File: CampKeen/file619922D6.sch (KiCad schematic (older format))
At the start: 50 parts, among them Q20 2N7000, Q21 2N7000, Q22 2N7000, Q23 2N7000, Q24 2N7000, Q25 2N7000, Q26 2N7000, Q27 2N7000, Q28 2N7000, Q29 2N7000

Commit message: schematic done for Input isolation updates.
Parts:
- removed D10, D11, D12, D13, D3, D6, D7, D8, D9: 1N4004, Diode_THT:D_DO-41_SOD81_P10.16mm_Horizontal, symbol Diode:1N4004
- removed R70, R71, R72, R76, R77, R78: 1M, Resistor_THT:R_Axial_DIN0207_L6.3mm_D2.5mm_P2.54mm_Vertical, symbol Device:R
- added D? (x9): 1N4007, Diode_THT:D_DO-41_SOD81_P10.16mm_Horizontal, symbol Diode:1N4007
- added IC? (x2): LTV-814, DIP762W60P254L460H450Q4N, symbol SamacSys_Parts:LTV-814
- added Q? (x2): LTV-847, DIP762W60P254L1984H450Q16N, symbol SamacSys_Parts:LTV-847
- added R? (x10): 22k, Resistor_THT:R_Axial_DIN0207_L6.3mm_D2.5mm_P2.54mm_Vertical, symbol Device:R
- added R? (x5): 330, Resistor_THT:R_Axial_DIN0207_L6.3mm_D2.5mm_P2.54mm_Vertical, symbol Device:R
- added R?: 300, Resistor_THT:R_Axial_DIN0207_L6.3mm_D2.5mm_P2.54mm_Vertical, symbol Device:R
- D5: value 1N4004 -> 1N4007; symbol Diode:1N4004 -> Diode:1N4007
- R63, R64, R66: value 1M -> 330
- R65: value 1M -> 300
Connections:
- net labels added: +5V
- wire segments 129 -> 207
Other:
- moved on the sheet: C28, C29, C30, C31, C32, C33, C34, C35, C36, C37, D5, Q20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

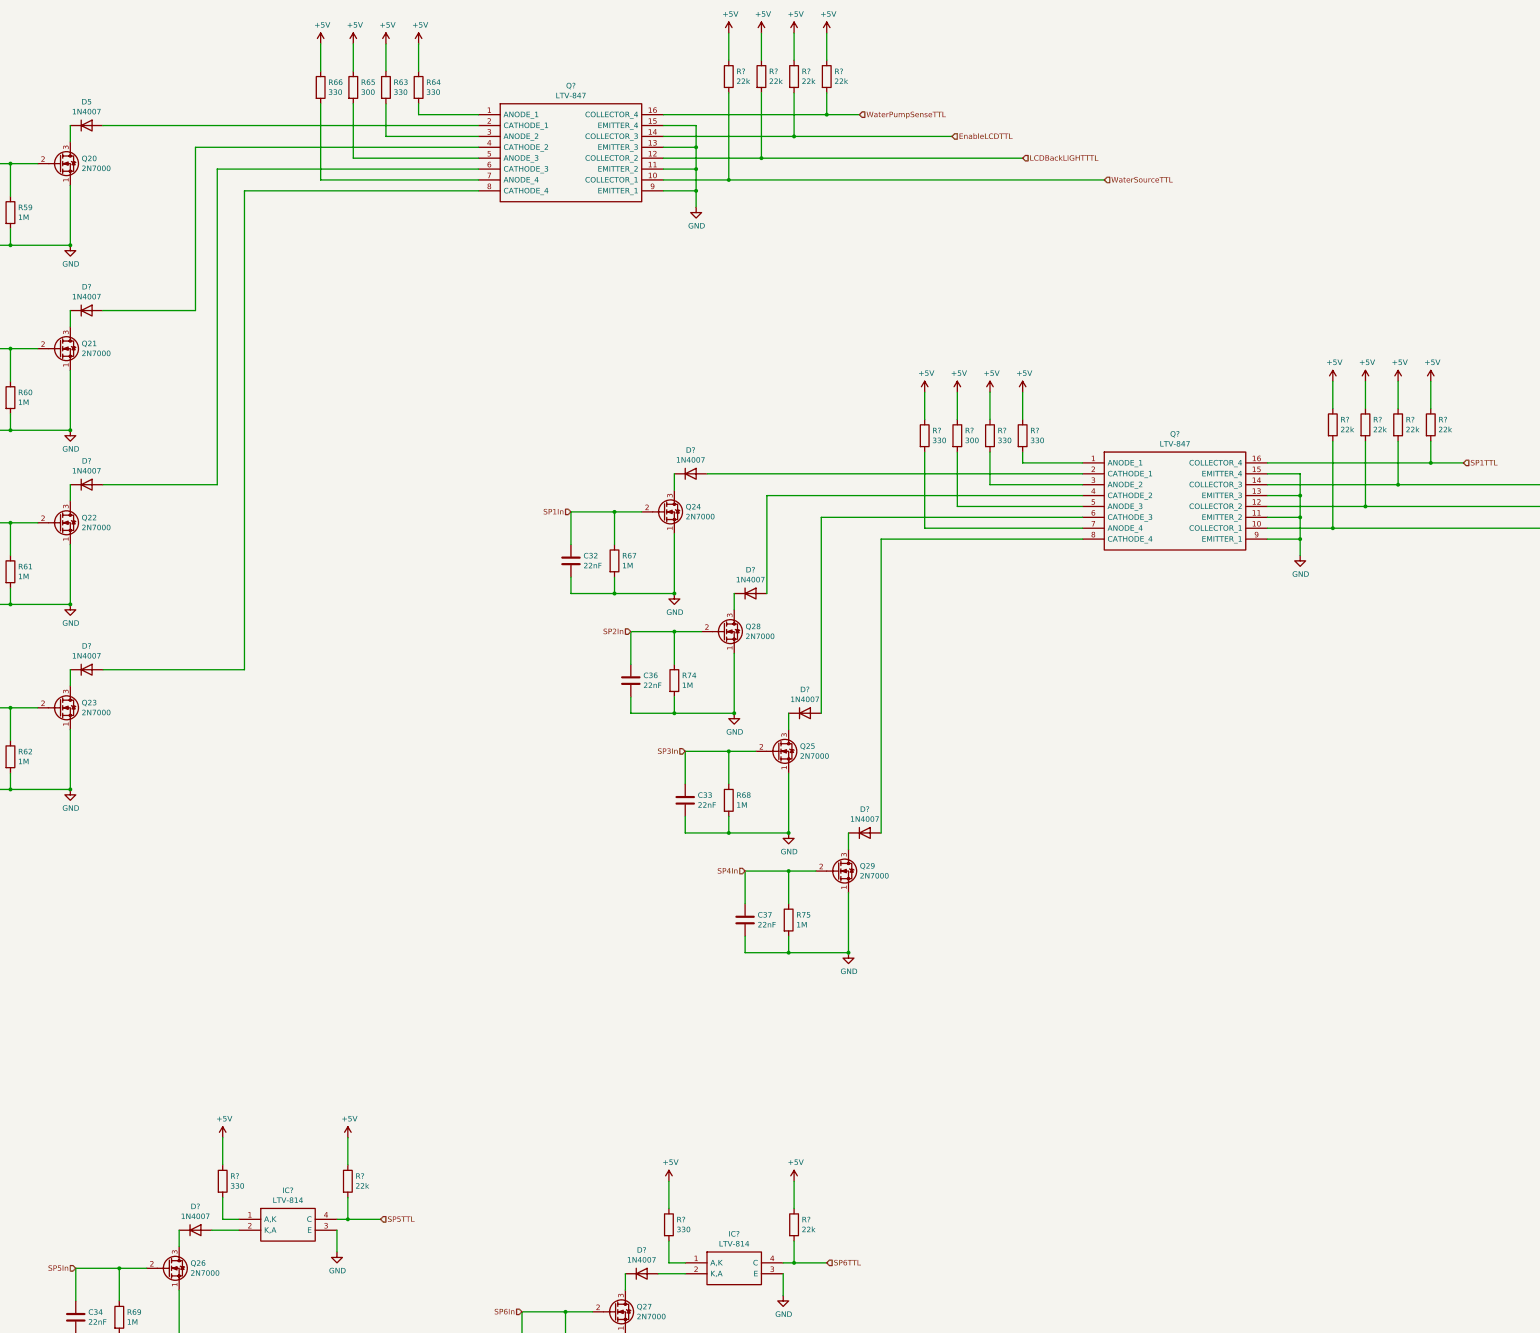
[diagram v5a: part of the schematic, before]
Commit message: added the appropriate power flags to the voltage rails as to make DRC Happy.
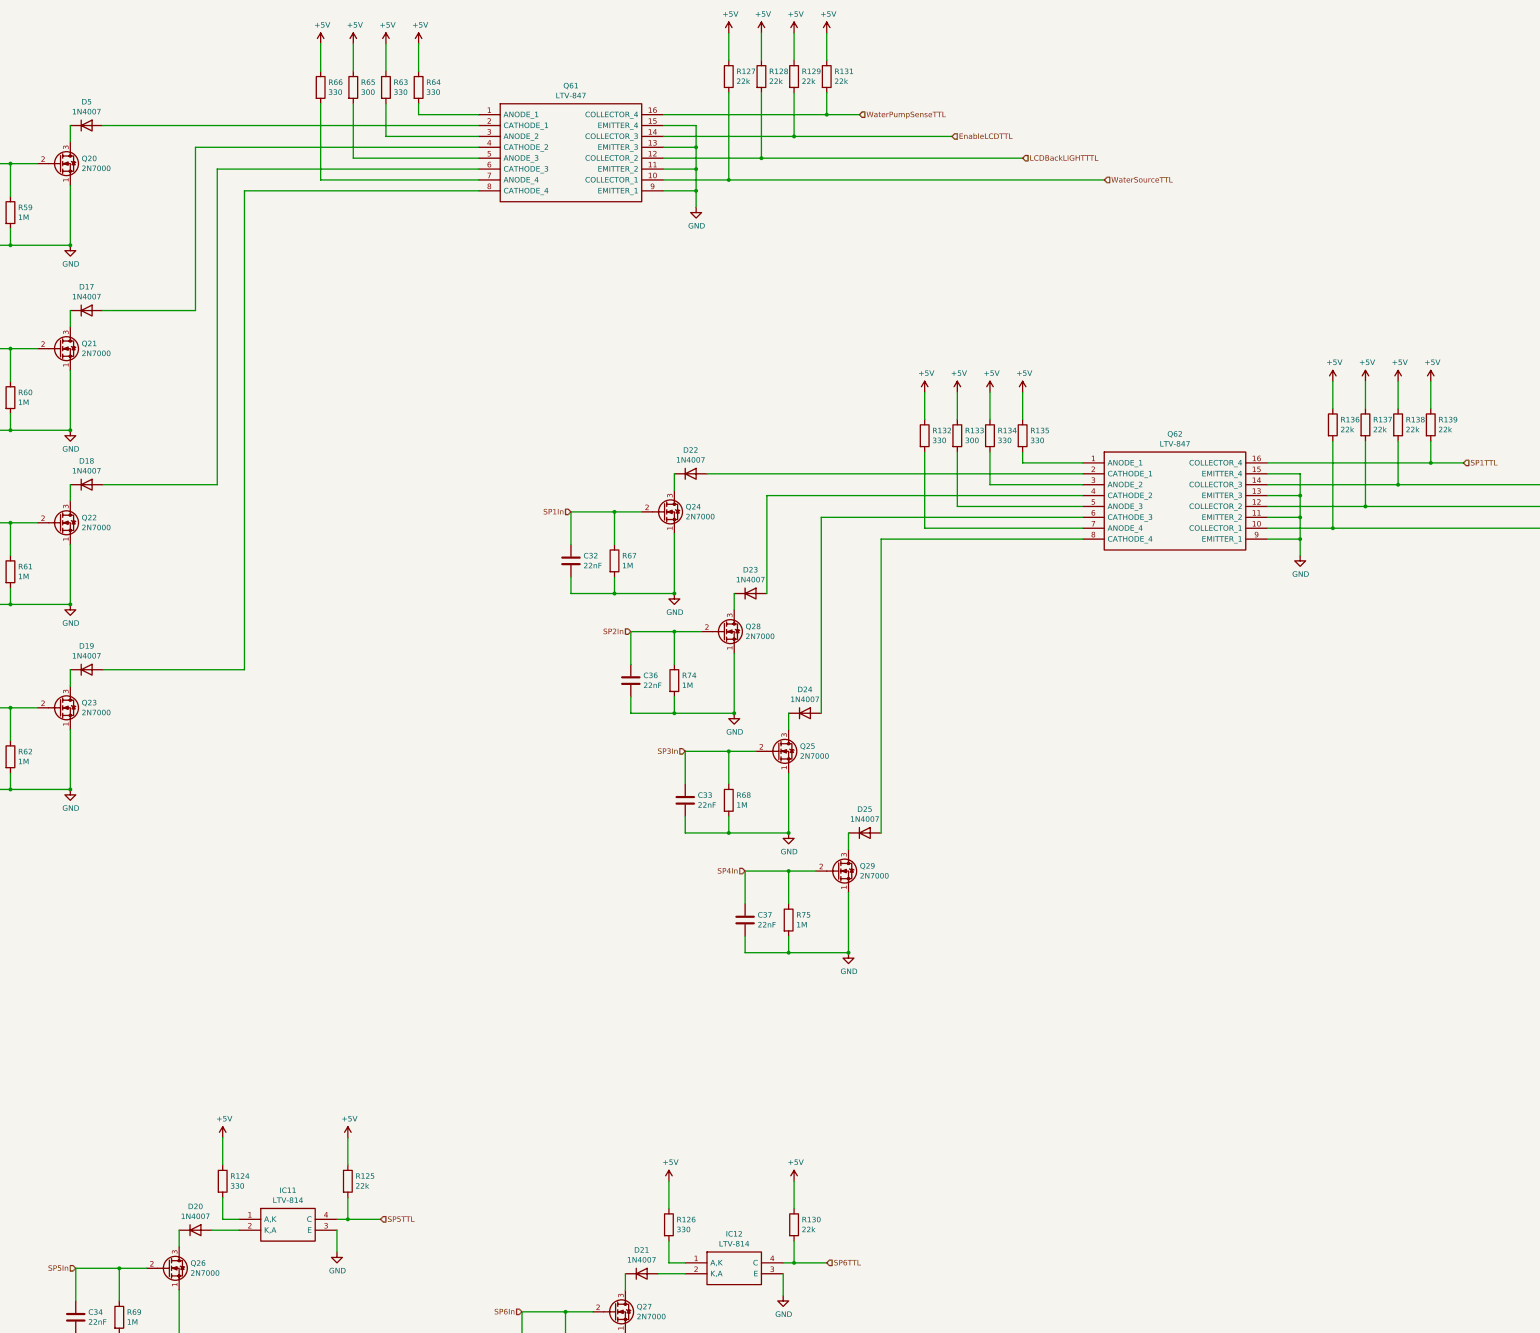
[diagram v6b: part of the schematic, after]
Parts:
- gave numbers to parts that had none: 29
